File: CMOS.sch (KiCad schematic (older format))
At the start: 7 parts, among them U24 PAL16L8, U25 28F010, U26 28F010

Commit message: Started PCB
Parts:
- C29: renamed from C28; footprint (none) -> Capacitor_SMD:CP_Elec_3x5.3
- C30: renamed from C29; footprint (none) -> Capacitor_SMD:CP_Elec_3x5.3
- C31: renamed from C30; footprint (none) -> Capacitor_SMD:CP_Elec_3x5.3
- C32: renamed from C31; footprint (none) -> Capacitor_SMD:CP_Elec_3x5.3
- U22: renamed from U24; footprint (none) -> Package_DIP:DIP-20_W7.62mm
- U23: renamed from U25; footprint 28F010 -> Package_DIP:DIP-32_W7.62mm
- U24: renamed from U26; footprint 28F010 -> parts:28F010
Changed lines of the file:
@@
 $EndDescr
 $Comp
-L 28F010:28F010 U25
+L 28F010:28F010 U23
 U 1 1 61B78CA0
 P 6450 1050
-F 0 "U25" H 7550 1437 60  0000 C CNN
+F 0 "U23" H 7550 1437 60  0000 C CNN
 F 1 "28F010" H 7550 1331 60  0000 C CNN
-F 2 "28F010" H 7550 1290 60  0001 C CNN
+F 2 "Package_DIP:DIP-32_W7.62mm" H 7550 1290 60  0001 C CNN
 F 3 "" H 6450 1050 60  0000 C CNN
 	1    6450 1050
@@
 $EndComp
 $Comp
-L power:+12V #PWR0116
+L power:+12V #PWR0107
 U 1 1 61B8538B
 P 6450 850
-F 0 "#PWR0116" H 6450 700 50  0001 C CNN
+F 0 "#PWR0107" H 6450 700 50  0001 C CNN
 F 1 "+12V" H 6465 1023 50  0000 C CNN
 F 2 "" H 6450 850 50  0001 C CNN
@@
 $EndComp
 $Comp
-L power:+5V #PWR0117
+L power:+5V #PWR0111
 U 1 1 61B86FF6
 P 8700 1050
-F 0 "#PWR0117" H 8700 900 50  0001 C CNN
+F 0 "#PWR0111" H 8700 900 50  0001 C CNN
 F 1 "+5V" H 8715 1223 50  0000 C CNN
 F 2 "" H 8700 1050 50  0001 C CNN
@@
 $EndComp
 $Comp
-L power:GND #PWR0118
+L power:GND #PWR0109
 U 1 1 61B89255
 P 7250 3050
-F 0 "#PWR0118" H 7250 2800 50  0001 C CNN
+F 0 "#PWR0109" H 7250 2800 50  0001 C CNN
 F 1 "GND" H 7255 2877 50  0000 C CNN
 F 2 "" H 7250 3050 50  0001 C CNN
@@
 $EndComp
 $Comp
-L Device:C C28
+L Device:C C29
 U 1 1 61B8A603
 P 6700 3050
-F 0 "C28" V 6448 3050 50  0000 C CNN
+F 0 "C29" V 6448 3050 50  0000 C CNN
 F 1 ".0000001" V 6539 3050 50  0000 C CNN
-F 2 "" H 6738 2900 50  0001 C CNN
+F 2 "Capacitor_SMD:CP_Elec_3x5.3" H 6738 2900 50  0001 C CNN
 F 3 "~" H 6700 3050 50  0001 C CNN
 	1    6700 3050
@@
 $EndComp
 $Comp
-L Device:C C30
+L Device:C C31
 U 1 1 61B8C95B
 P 7900 3050
-F 0 "C30" V 7648 3050 50  0000 C CNN
+F 0 "C31" V 7648 3050 50  0000 C CNN
 F 1 ".0000001" V 7739 3050 50  0000 C CNN
-F 2 "" H 7938 2900 50  0001 C CNN
+F 2 "Capacitor_SMD:CP_Elec_3x5.3" H 7938 2900 50  0001 C CNN
 F 3 "~" H 7900 3050 50  0001 C CNN
 	1    7900 3050
@@
 Connection ~ 9000 3550
 $Comp
-L Logic_Programmable:PAL16L8 U24
+L Logic_Programmable:PAL16L8 U22
 U 1 1 61BBEFCA
 P 5000 3450
-F 0 "U24" H 5000 4331 50  0000 C CNN
+F 0 "U22" H 5000 4331 50  0000 C CNN
 F 1 "PAL16L8" H 5000 4240 50  0000 C CNN
-F 2 "" H 5000 3450 50  0001 C CNN
+F 2 "Package_DIP:DIP-20_W7.62mm" H 5000 3450 50  0001 C CNN
 F 3 "" H 5000 3450 50  0001 C CNN
 	1    5000 3450
@@
 $EndComp
 $Comp
-L power:+5V #PWR0119
+L power:+5V #PWR0105
 U 1 1 61BC2C82
 P 5000 2750
-F 0 "#PWR0119" H 5000 2600 50  0001 C CNN
+F 0 "#PWR0105" H 5000 2600 50  0001 C CNN
 F 1 "+5V" V 5015 2878 50  0000 L CNN
 F 2 "" H 5000 2750 50  0001 C CNN
@@
 $EndComp
 $Comp
-L power:GND #PWR0120
+L power:GND #PWR0106
 U 1 1 61BC39FB
 P 5000 4050
-F 0 "#PWR0120" H 5000 3800 50  0001 C CNN
+F 0 "#PWR0106" H 5000 3800 50  0001 C CNN
 F 1 "GND" H 5005 3877 50  0000 C CNN
 F 2 "" H 5000 4050 50  0001 C CNN
@@
 	8650 1050 8700 1050
 $Comp
-L 28F010:28F010 U26
+L 28F010:28F010 U24
 U 1 1 61BD82F2
 P 6500 4300
-F 0 "U26" H 7600 4687 60  0000 C CNN
+F 0 "U24" H 7600 4687 60  0000 C CNN
 F 1 "28F010" H 7600 4581 60  0000 C CNN
-F 2 "28F010" H 7600 4540 60  0001 C CNN
+F 2 "parts:28F010" H 7600 4540 60  0001 C CNN
 F 3 "" H 6500 4300 60  0000 C CNN
 	1    6500 4300
@@
 $EndComp
 $Comp
-L power:+12V #PWR0121
+L power:+12V #PWR0108
 U 1 1 61BD843C
 P 6500 4100
-F 0 "#PWR0121" H 6500 3950 50  0001 C CNN
+F 0 "#PWR0108" H 6500 3950 50  0001 C CNN
 F 1 "+12V" H 6515 4273 50  0000 C CNN
 F 2 "" H 6500 4100 50  0001 C CNN
@@
 $EndComp
 $Comp
-L power:+5V #PWR0122
+L power:+5V #PWR0112
 U 1 1 61BD8446
 P 8750 4300
-F 0 "#PWR0122" H 8750 4150 50  0001 C CNN
+F 0 "#PWR0112" H 8750 4150 50  0001 C CNN
 F 1 "+5V" H 8765 4473 50  0000 C CNN
 F 2 "" H 8750 4300 50  0001 C CNN
@@
 $EndComp
 $Comp
-L power:GND #PWR0123
+L power:GND #PWR0110
 U 1 1 61BD8450
 P 7300 6300
-F 0 "#PWR0123" H 7300 6050 50  0001 C CNN
+F 0 "#PWR0110" H 7300 6050 50  0001 C CNN
 F 1 "GND" H 7305 6127 50  0000 C CNN
 F 2 "" H 7300 6300 50  0001 C CNN
@@
 $EndComp
 $Comp
-L Device:C C29
+L Device:C C30
 U 1 1 61BD845A
 P 6750 6300
-F 0 "C29" V 6498 6300 50  0000 C CNN
+F 0 "C30" V 6498 6300 50  0000 C CNN
 F 1 ".0000001" V 6589 6300 50  0000 C CNN
-F 2 "" H 6788 6150 50  0001 C CNN
+F 2 "Capacitor_SMD:CP_Elec_3x5.3" H 6788 6150 50  0001 C CNN
 F 3 "~" H 6750 6300 50  0001 C CNN
 	1    6750 6300
@@
 $EndComp
 $Comp
-L Device:C C31
+L Device:C C32
 U 1 1 61BD8464
 P 7950 6300
-F 0 "C31" V 7698 6300 50  0000 C CNN
+F 0 "C32" V 7698 6300 50  0000 C CNN
 F 1 ".0000001" V 7789 6300 50  0000 C CNN
-F 2 "" H 7988 6150 50  0001 C CNN
+F 2 "Capacitor_SMD:CP_Elec_3x5.3" H 7988 6150 50  0001 C CNN
 F 3 "~" H 7950 6300 50  0001 C CNN
 	1    7950 6300

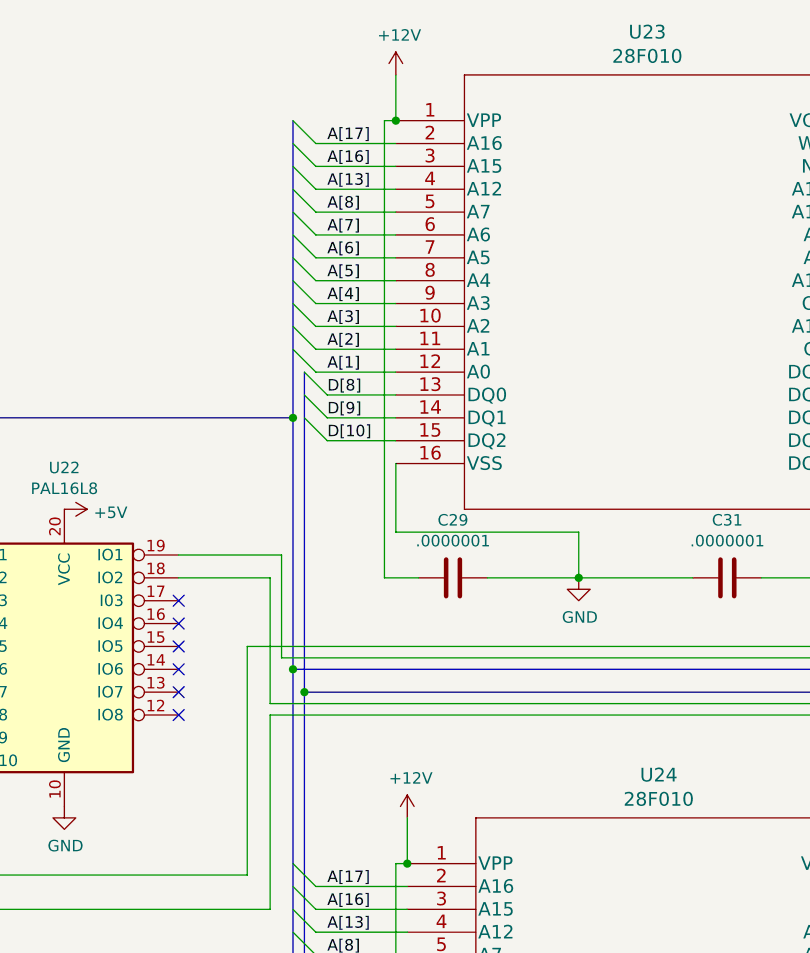
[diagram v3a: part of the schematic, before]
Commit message: CMOS power fix
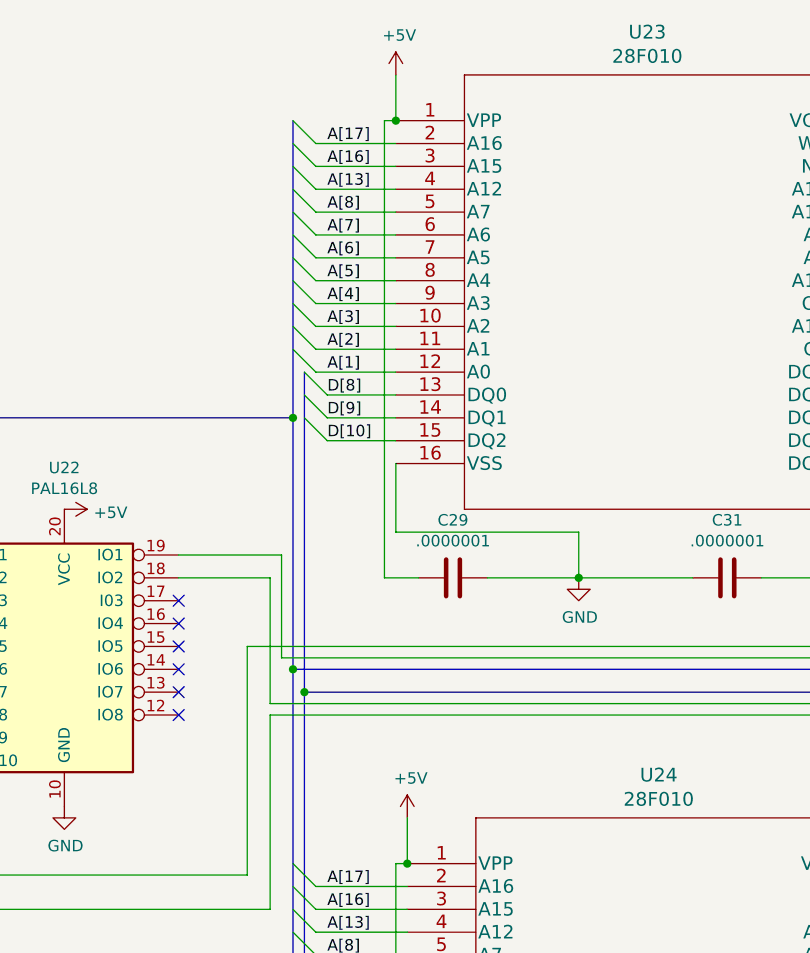
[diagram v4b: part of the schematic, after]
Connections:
- net +12V is gone; now on net +5V: C29.2, C30.2, U23.1 (VPP), U24.1 (VPP)
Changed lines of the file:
@@
-$EndComp
-$Comp
-L power:+12V #PWR0107
-U 1 1 61B8538B
-P 6450 850
-F 0 "#PWR0107" H 6450 700 50  0001 C CNN
-F 1 "+12V" H 6465 1023 50  0000 C CNN
-F 2 "" H 6450 850 50  0001 C CNN
-F 3 "" H 6450 850 50  0001 C CNN
-	1    6450 850
-	1    0    0    -1
 $EndComp
 $Comp
@@
 F 3 "" H 6500 4300 60  0000 C CNN
 	1    6500 4300
-	1    0    0    -1
-$EndComp
-$Comp
-L power:+12V #PWR0108
-U 1 1 61BD843C
-P 6500 4100
-F 0 "#PWR0108" H 6500 3950 50  0001 C CNN
-F 1 "+12V" H 6515 4273 50  0000 C CNN
-F 2 "" H 6500 4100 50  0001 C CNN
-F 3 "" H 6500 4100 50  0001 C CNN
-	1    6500 4100
 	1    0    0    -1
 $EndComp
@@
 Wire Bus Line
 	9000 3550 9000 5900
+$Comp
+L power:+5V #PWR?
+U 1 1 61C1A31D
+P 6500 4100
+F 0 "#PWR?" H 6500 3950 50  0001 C CNN
+F 1 "+5V" H 6515 4273 50  0000 C CNN
+F 2 "" H 6500 4100 50  0001 C CNN
+F 3 "" H 6500 4100 50  0001 C CNN
+	1    6500 4100
+	1    0    0    -1
+$EndComp
+$Comp
+L power:+5V #PWR?
+U 1 1 61C1A596
+P 6450 850
+F 0 "#PWR?" H 6450 700 50  0001 C CNN
+F 1 "+5V" H 6465 1023 50  0000 C CNN
+F 2 "" H 6450 850 50  0001 C CNN
+F 3 "" H 6450 850 50  0001 C CNN
+	1    6450 850
+	1    0    0    -1
+$EndComp
 $EndSCHEMATC
